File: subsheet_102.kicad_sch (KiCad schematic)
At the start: 7 parts, among them U102 EPROM_32_PINS_DIP_PHY, U103 EPROM_32_PINS_DIP_PHY

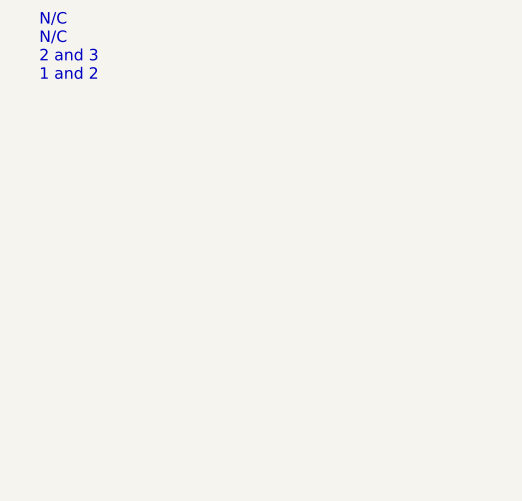
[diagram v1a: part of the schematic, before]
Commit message: add gnd/vcc symbol to start replacing local labels
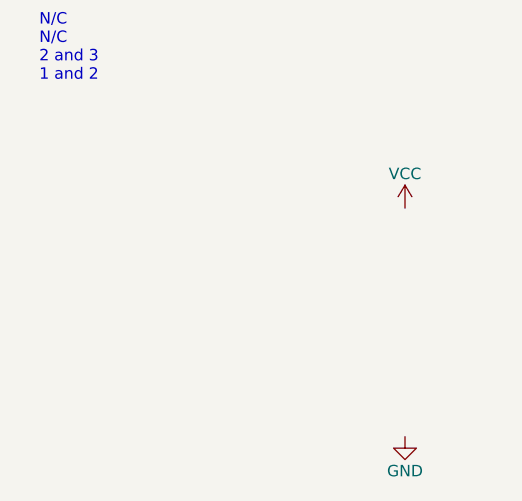
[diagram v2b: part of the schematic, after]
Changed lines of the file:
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@@
     (pin "3")
   )
+  (symbol (lib_id "power:VCC") (at 171.45 170.18 0) (unit 1)
+    (in_bom yes) (on_board yes)
+    (property "Reference" "#PWR?" (id 0) (at 171.45 173.99 0)
+      (effects (font (size 1.27 1.27)) hide)
+    )
+    (property "Value" "VCC" (id 1) (at 171.45 166.37 0))
+    (property "Footprint" "" (id 2) (at 171.45 170.18 0)
+      (effects (font (size 1.27 1.27)) hide)
+    )
+    (property "Datasheet" "" (id 3) (at 171.45 170.18 0)
+      (effects (font (size 1.27 1.27)) hide)
+    )
+    (pin "1")
+  )
+  (symbol (lib_id "power:GND") (at 171.45 195.58 0) (unit 1)
+    (in_bom yes) (on_board yes)
+    (property "Reference" "#PWR?" (id 0) (at 171.45 201.93 0)
+      (effects (font (size 1.27 1.27)) hide)
+    )
+    (property "Value" "GND" (id 1) (at 171.45 199.39 0))
+    (property "Footprint" "" (id 2) (at 171.45 195.58 0)
+      (effects (font (size 1.27 1.27)) hide)
+    )
+    (property "Datasheet" "" (id 3) (at 171.45 195.58 0)
+      (effects (font (size 1.27 1.27)) hide)
+    )
+    (pin "1")
+  )
 )
